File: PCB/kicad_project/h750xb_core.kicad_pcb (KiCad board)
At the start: 6 copper layers, 50 x 35 mm, 93 parts, among them J1 DF40C-100DP-0.4V_51_, J2 DF40C-100DP-0.4V_51_, U1 STM32H750XBHx, U2 TPS74801DRC, U3 TPS82130, U4 REF3020, U7 W25Q32JVZP, U8 W25Q32JVZP, Y1 32M, Y2 32.768k

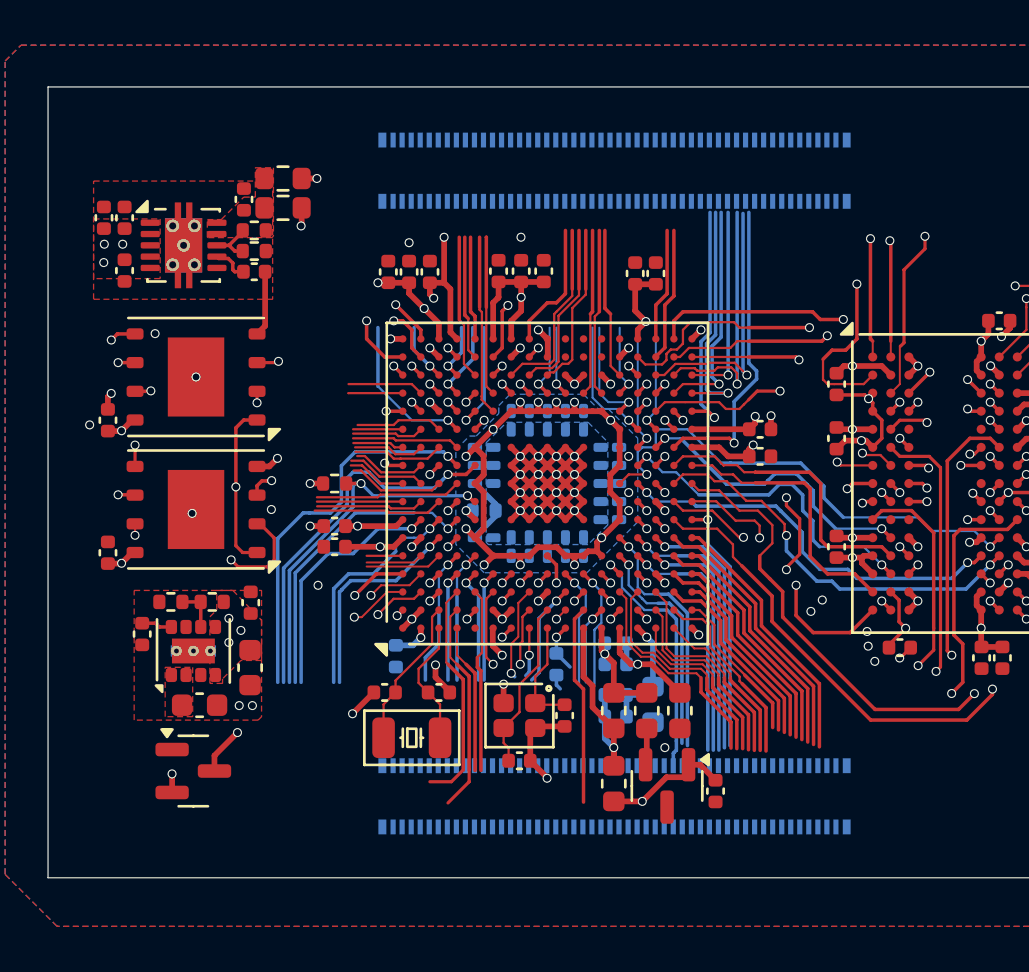
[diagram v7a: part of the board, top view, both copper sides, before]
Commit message: 更新原理图网络和PCB部分IO走线
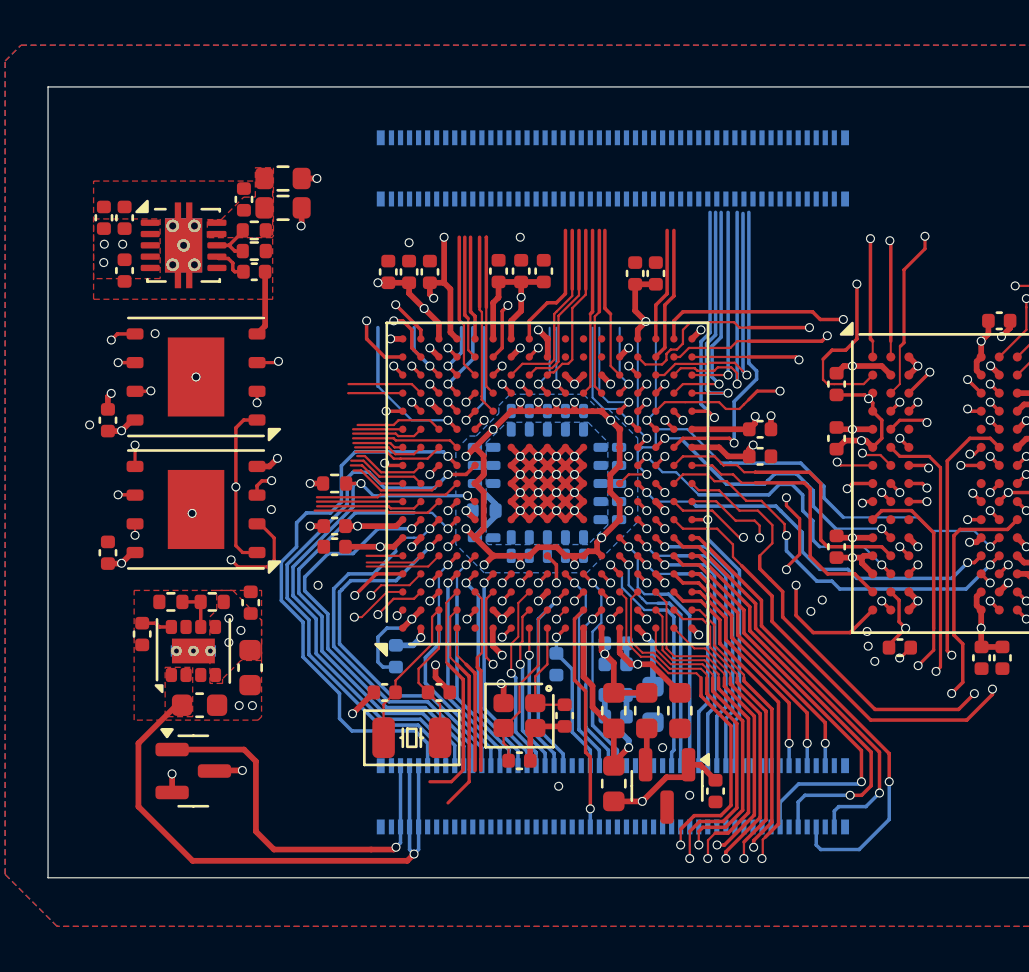
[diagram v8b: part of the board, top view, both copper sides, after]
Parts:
- moved J1 0.12 mm to (40.3, 80.3)
- moved J2 0.07 mm to (40.3, 108.1)
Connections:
- C22 pad 1: /mcu/NRST -> /NRST
- J2 pad 1: unconnected-(J2-Pad1) -> /mcu/PJ2
- J2 pad 12: unconnected-(J2-Pad12) -> /PA4
- J2 pad 13: unconnected-(J2-Pad13) -> /PB1
- J2 pad 24: unconnected-(J2-Pad24) -> /mcu/PJ4
- J2 pad 26: unconnected-(J2-Pad26) -> /PB2
- J2 pad 28: unconnected-(J2-Pad28) -> /mcu/PJ1
- J2 pad 30: unconnected-(J2-Pad30) -> /PA7
- J2 pad 32: unconnected-(J2-Pad32) -> /mcu/PI15
- J2 pad 34: unconnected-(J2-Pad34) -> /mcu/PJ0
- J2 pad 36: unconnected-(J2-Pad36) -> /PA0
- J2 pad 38: unconnected-(J2-Pad38) -> /PA1
- J2 pad 4: unconnected-(J2-Pad4) -> /PC5
- J2 pad 40: unconnected-(J2-Pad40) -> GND
- J2 pad 42: unconnected-(J2-Pad42) -> GND
- J2 pad 5: unconnected-(J2-Pad5) -> /mcu/PJ3
- J2 pad 50: unconnected-(J2-Pad50) -> /PF9
- J2 pad 52: unconnected-(J2-Pad52) -> /PC1
- J2 pad 54: unconnected-(J2-Pad54) -> /PF8
- J2 pad 55: unconnected-(J2-Pad55) -> /PC0
- J2 pad 56: unconnected-(J2-Pad56) -> /NRST
- J2 pad 58: unconnected-(J2-Pad58) -> GND
- J2 pad 60: unconnected-(J2-Pad60) -> GND
- J2 pad 62: unconnected-(J2-Pad62) -> /PF7
- J2 pad 64: unconnected-(J2-Pad64) -> /mcu/PI12
- J2 pad 66: unconnected-(J2-Pad66) -> /mcu/PI13
- J2 pad 68: unconnected-(J2-Pad68) -> /mcu/PI14
- J2 pad 70: unconnected-(J2-Pad70) -> /mcu/PI11
- J2 pad 72: unconnected-(J2-Pad72) -> /mcu/PI8
- J2 pad 74: unconnected-(J2-Pad74) -> /PE6
- J2 pad 76: unconnected-(J2-Pad76) -> /PB9
- J2 pad 78: unconnected-(J2-Pad78) -> /PB8
- J2 pad 8: unconnected-(J2-Pad8) -> /PC4
- J2 pad 80: unconnected-(J2-Pad80) -> /PB3
- J2 pad 82: unconnected-(J2-Pad82) -> /mcu/PK6
- J2 pad 84: unconnected-(J2-Pad84) -> /PB4
- J2 pad 86: unconnected-(J2-Pad86) -> /mcu/PK7
- J2 pad 88: unconnected-(J2-Pad88) -> /BOOT0
- J2 pad 9: unconnected-(J2-Pad9) -> /PB0
- J2 pad 90: unconnected-(J2-Pad90) -> /mcu/PJ13
- J2 pad 92: unconnected-(J2-Pad92) -> /mcu/PJ14
- J2 pad 93: unconnected-(J2-Pad93) -> VBUS
- J2 pad 94: unconnected-(J2-Pad94) -> VBUS
- J2 pad 95: unconnected-(J2-Pad95) -> VBUS
- J2 pad 96: unconnected-(J2-Pad96) -> VBUS
- J2 pad 97: unconnected-(J2-Pad97) -> /ex_VBAT
- J2 pad 98: unconnected-(J2-Pad98) -> /ex_VBAT
- R2 pad 1: /mcu/BOOT0 -> /BOOT0
- U1 pad A11: unconnected-(U1-PD5-PadA11) -> /PD5
- U1 pad A12: unconnected-(U1-PD4-PadA12) -> /PD4
- U1 pad A14: unconnected-(U1-PA15-PadA14) -> /PA15
- U1 pad A5: unconnected-(U1-PB5-PadA5) -> /PB5
- U1 pad A8: unconnected-(U1-PK5-PadA8) -> /mcu/PK5
- U1 pad A9: unconnected-(U1-PG10-PadA9) -> /mcu/PG10
- U1 pad B10: unconnected-(U1-PJ15-PadB10) -> /mcu/PJ15
- U1 pad B11: unconnected-(U1-PD6-PadB11) -> /PD6
- U1 pad B12: unconnected-(U1-PD3-PadB12) -> /PD3
- U1 pad B14: unconnected-(U1-PA14-PadB14) -> /PA14
- U1 pad B5: unconnected-(U1-PB6-PadB5) -> /PB6
- U1 pad B7: unconnected-(U1-PB4-PadB7) -> /PB4
- U1 pad B8: unconnected-(U1-PK4-PadB8) -> /mcu/PK4
- U1 pad B9: unconnected-(U1-PG11-PadB9) -> /mcu/PG11
- U1 pad C11: unconnected-(U1-PD7-PadC11) -> /PD7
- U1 pad C12: unconnected-(U1-PC12-PadC12) -> /PC12
- U1 pad C15: unconnected-(U1-PA13-PadC15) -> /PA13
- U1 pad C5: unconnected-(U1-PB7-PadC5) -> /PB7
- U1 pad C6: unconnected-(U1-PB3-PadC6) -> /PB3
- U1 pad C7: unconnected-(U1-PK6-PadC7) -> /mcu/PK6
- U1 pad C8: unconnected-(U1-PK3-PadC8) -> /mcu/PK3
- U1 pad C9: unconnected-(U1-PG12-PadC9) -> /mcu/PG12
- U1 pad D1: unconnected-(U1-PE5-PadD1) -> /PE5
- U1 pad D10: unconnected-(U1-PJ14-PadD10) -> /mcu/PJ14
- U1 pad D11: unconnected-(U1-PJ12-PadD11) -> /mcu/PJ12
- U1 pad D12: unconnected-(U1-PD2-PadD12) -> /PD2
- U1 pad D14: unconnected-(U1-PA10-PadD14) -> /PA10
- U1 pad D15: unconnected-(U1-PA9-PadD15) -> /PA9
- U1 pad D2: unconnected-(U1-PE4-PadD2) -> /PE4
- U1 pad D3: unconnected-(U1-PE3-PadD3) -> /PE3
- U1 pad D4: unconnected-(U1-PB9-PadD4) -> /PB9
- U1 pad D5: unconnected-(U1-PB8-PadD5) -> /PB8
- U1 pad D7: unconnected-(U1-PK7-PadD7) -> /mcu/PK7
- U1 pad D9: unconnected-(U1-PG13-PadD9) -> /mcu/PG13
- U1 pad E10: unconnected-(U1-PJ13-PadE10) -> /mcu/PJ13
- U1 pad E13: unconnected-(U1-PC8-PadE13) -> /PC8
- U1 pad E15: unconnected-(U1-PA8-PadE15) -> /PA8
- U1 pad E16: unconnected-(U1-PA12-PadE16) -> /PA12
- U1 pad E17: unconnected-(U1-PA11-PadE17) -> /PA11
- U1 pad E3: unconnected-(U1-PC13-PadE3) -> /PC13
- U1 pad E4: unconnected-(U1-PI8-PadE4) -> /mcu/PI8
- U1 pad E5: unconnected-(U1-PE6-PadE5) -> /PE6
- U1 pad E8: /mcu/BOOT0 -> /BOOT0
- U1 pad F13: unconnected-(U1-PC7-PadF13) -> /PC7
- U1 pad F14: unconnected-(U1-PC6-PadF14) -> /PC6
- U1 pad F16: unconnected-(U1-PG7-PadF16) -> /mcu/PG7
- U1 pad F4: unconnected-(U1-PI11-PadF4) -> /mcu/PI11
- U1 pad G15: unconnected-(U1-PG6-PadG15) -> /mcu/PG6
- U1 pad H1: unconnected-(U1-PI12-PadH1) -> /mcu/PI12
- U1 pad H15: unconnected-(U1-PG3-PadH15) -> /mcu/PG3
- U1 pad H17: unconnected-(U1-PK2-PadH17) -> /mcu/PK2
- U1 pad H2: unconnected-(U1-PI13-PadH2) -> /mcu/PI13
- U1 pad H3: unconnected-(U1-PI14-PadH3) -> /mcu/PI14
- U1 pad J14: unconnected-(U1-PK0-PadJ14) -> /mcu/PK0
- U1 pad J15: unconnected-(U1-PK1-PadJ15) -> /mcu/PK1
- U1 pad K1: /mcu/NRST -> /NRST
- U1 pad K14: unconnected-(U1-PJ11-PadK14) -> /mcu/PJ11
- U1 pad K3: unconnected-(U1-PF7-PadK3) -> /PF7
- U1 pad K4: unconnected-(U1-PF8-PadK4) -> /PF8
- U1 pad L14: unconnected-(U1-PJ10-PadL14) -> /mcu/PJ10
- U1 pad L2: unconnected-(U1-PC0-PadL2) -> /PC0
- U1 pad L4: unconnected-(U1-PF9-PadL4) -> /PF9
- U1 pad M14: unconnected-(U1-PJ9-PadM14) -> /mcu/PJ9
- U1 pad M2: unconnected-(U1-PC1-PadM2) -> /PC1
- U1 pad N13: unconnected-(U1-PJ8-PadN13) -> /mcu/PJ8
- U1 pad N14: unconnected-(U1-PJ7-PadN14) -> /mcu/PJ7
- U1 pad N15: unconnected-(U1-PJ6-PadN15) -> /mcu/PJ6
- U1 pad N3: unconnected-(U1-PA2-PadN3) -> /PA2
- U1 pad N4: unconnected-(U1-PA1-PadN4) -> /PA1
- U1 pad N5: unconnected-(U1-PA0-PadN5) -> /PA0
- U1 pad N6: unconnected-(U1-PJ0-PadN6) -> /mcu/PJ0
- U1 pad P11: unconnected-(U1-PB10-PadP11) -> /PB10
- U1 pad P12: unconnected-(U1-PB11-PadP12) -> /PB11
- U1 pad P3: unconnected-(U1-PH4-PadP3) -> /mcu/PH4
- U1 pad P5: unconnected-(U1-PI15-PadP5) -> /mcu/PI15
- U1 pad P6: unconnected-(U1-PJ1-PadP6) -> /mcu/PJ1
- U1 pad R1: unconnected-(U1-PC2_C-PadR1) -> /PC2_C
- U1 pad R12: unconnected-(U1-PJ5-PadR12) -> /mcu/PJ5
- U1 pad R15: unconnected-(U1-PD11-PadR15) -> /PD11
- U1 pad R16: unconnected-(U1-PD12-PadR16) -> /PD12
- U1 pad R17: unconnected-(U1-PD13-PadR17) -> /PD13
- U1 pad R2: unconnected-(U1-PC3_C-PadR2) -> /PC3_C
- U1 pad R3: unconnected-(U1-PA6-PadR3) -> /PA6
- U1 pad R5: unconnected-(U1-PA7-PadR5) -> /PA7
- U1 pad R6: unconnected-(U1-PB2-PadR6) -> /PB2
- U1 pad T1: unconnected-(U1-PA0_C-PadT1) -> /PA0_C
- U1 pad T11: unconnected-(U1-PH6-PadT11) -> /mcu/PH6
- U1 pad T14: unconnected-(U1-PB12-PadT14) -> /PB12
- U1 pad T15: unconnected-(U1-PB15-PadT15) -> /PB15
- U1 pad T2: unconnected-(U1-PA1_C-PadT2) -> /PA1_C
- U1 pad T3: unconnected-(U1-PA5-PadT3) -> /PA5
- U1 pad T4: unconnected-(U1-PC4-PadT4) -> /PC4
- U1 pad T5: unconnected-(U1-PB1-PadT5) -> /PB1
- U1 pad T6: unconnected-(U1-PJ2-PadT6) -> /mcu/PJ2
- U1 pad U13: unconnected-(U1-PH7-PadU13) -> /mcu/PH7
- U1 pad U14: unconnected-(U1-PB13-PadU14) -> /PB13
- U1 pad U15: unconnected-(U1-PB14-PadU15) -> /PB14
- U1 pad U2: unconnected-(U1-PA3-PadU2) -> /PA3
- U1 pad U3: unconnected-(U1-PA4-PadU3) -> /PA4
- U1 pad U4: unconnected-(U1-PC5-PadU4) -> /PC5
- U1 pad U5: unconnected-(U1-PB0-PadU5) -> /PB0
- U1 pad U6: unconnected-(U1-PJ3-PadU6) -> /mcu/PJ3
- U1 pad U7: unconnected-(U1-PJ4-PadU7) -> /mcu/PJ4
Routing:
- net VBUS: track 0.00 -> 26.7 mm, vias 0 -> 1
- net /mcu/PJ14: track 0.00 -> 24.9 mm, vias 0 -> 1
- net /mcu/PJ13: track 0.00 -> 24.0 mm, vias 0 -> 1
- net /BOOT0: track 0.00 -> 23.7 mm, vias 0 -> 2
- net /mcu/PK7: track 0.00 -> 21.0 mm, vias 0 -> 1
- net /mcu/PJ3: track 0.00 -> 20.9 mm, vias 0 -> 1
- net /PB1: track 0.00 -> 18.9 mm, vias 0 -> 1
- net /mcu/PJ2: track 0.00 -> 18.5 mm, vias 0 -> 1
- net /PB4: track 0.00 -> 18.5 mm, vias 0 -> 1
- net /PB0: track 0.00 -> 18.3 mm, vias 0 -> 1
- net /mcu/PK6: track 0.00 -> 17.5 mm, vias 0 -> 1
- net /ex_VBAT: track 0.00 -> 17.3 mm, vias 0 -> 1
- net unconnected-(U1-PJ14-PadD10): track 17.1 -> 0.00 mm, vias 1 -> 0
- net /PB3: track 0.00 -> 16.7 mm, vias 0 -> 1
- net unconnected-(U1-PJ13-PadE10): track 16.7 -> 0.00 mm, vias 1 -> 0
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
